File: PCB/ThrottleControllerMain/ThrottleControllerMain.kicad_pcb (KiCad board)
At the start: 2 copper layers, 39 parts, among them J1 Conn_ARM_JTAG_SWD_10, J2 Conn_01x02, J4 Conn_01x04_Pin, J5 Screw_Terminal_01x02, J6 Screw_Terminal_01x02, P1 USB_C_Plug, U1 RP2040, U2 TLV493D, U3 NCP1117-3.3_SOT223, U5 W25Q32JVSS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

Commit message: Updating PCB
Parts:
- C1, C16, C17, C18, C2, C4: footprint Capacitor_SMD:C_0805_2012Metric -> Capacitor_SMD:C_0603_1608Metric
- C11, C12, C13, C14, C15, C5, C6, C7, C8, C9: footprint Capacitor_SMD:C_0805_2012Metric -> Capacitor_SMD:C_0201_0603Metric
- P1: footprint Connector_USB:USB_C_Receptacle_Amphenol_12401548E4-2A -> Connector_USB:USB_C_Receptacle_G-Switch_GT-USB-7010ASV
- R1, R10, R2, R3, R4, R6, R7, R8, R9: footprint Resistor_SMD:R_0805_2012Metric -> Resistor_SMD:R_0603_1608Metric
- moved J4 59.7 mm to (106.2, 84.6), turned to 180 degrees
- moved J1 55.7 mm to (112.3, 76.2), turned to 0 degrees
- moved U2 53.8 mm to (131.1, 80.1)
- moved J2 46.0 mm to (134.6, 109.8), turned to -90 degrees
- moved J6 40.3 mm to (112.5, 69.3)
- moved R7 38.5 mm to (138.4, 103.3), turned to 90 degrees
- moved C3 33.7 mm to (123.3, 82.4), turned to -90 degrees
- moved C10 31.4 mm to (125.9, 82.4), turned to -90 degrees
- moved R5 27.6 mm to (135.9, 72.3)
- moved R2 24.5 mm to (130.8, 75.8), turned to 90 degrees
- moved U3 24.1 mm to (157.5, 99.1)
- moved R9 23.7 mm to (133.3, 75.8), turned to -90 degrees
- moved C17 23.3 mm to (139.1, 89.2), turned to -90 degrees
- moved R8 21.9 mm to (120.4, 82.1), turned to -90 degrees
- moved C14 21.1 mm to (134.6, 80.9)
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
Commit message: PCB footprint layout is mostly complete.
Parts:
- removed J6: Screw_Terminal_01x02, TerminalBlock_Phoenix:TerminalBlock_Phoenix_MPT-0,5-2-2.54_1x02_P2.54mm_Horizontal
- added H1: MountingHole, MountingHole:MountingHole_3.2mm_M3, F.Cu at (159.6, 108.9)
- added H2: MountingHole, MountingHole:MountingHole_3.2mm_M3, F.Cu at (140.2, 69.9)
- added H3: MountingHole, MountingHole:MountingHole_3.2mm_M3, F.Cu at (121.4, 69.9)
- added H4: MountingHole, MountingHole:MountingHole_3.2mm_M3, F.Cu at (140.2, 108.9)
- added J3: Conn_01x02_Socket, Connector_JST:JST_SH_BM02B-SRSS-TB_1x02-1MP_P1.00mm_Vertical, F.Cu at (120.1, 76.6)
- J1: value Conn_ARM_JTAG_SWD_10 -> Conn_01x03_Socket; footprint Connector_PinHeader_2.54mm:PinHeader_2x05_P2.54mm_Vertical -> Connector_JST:JST_SH_BM03B-SRSS-TB_1x03-1MP_P1.00mm_Vertical
- J5: value Screw_Terminal_01x02 -> Conn_01x02_Socket; footprint TerminalBlock_Phoenix:TerminalBlock_Phoenix_MPT-0,5-2-2.54_1x02_P2.54mm_Horizontal -> Connector_JST:JST_SH_BM02B-SRSS-TB_1x02-1MP_P1.00mm_Vertical
- R5: footprint Resistor_SMD:R_0805_2012Metric -> Resistor_SMD:R_0603_1608Metric
- Y1: footprint Crystal:Crystal_SMD_5032-2Pin_5.0x3.2mm -> Crystal:Crystal_SMD_3225-4Pin_3.2x2.5mm
- moved J4 44.0 mm to (148.6, 96.3)
- moved J1 29.9 mm to (142.1, 77.5), turned to -90 degrees
- moved R7 23.7 mm to (126.6, 82.8)
- moved R8 22.5 mm to (142.2, 87.8), turned to 180 degrees
- moved C5 22.4 mm to (136.7, 80.9), turned to 90 degrees
- moved C1 20.0 mm to (157.6, 104.3), turned to 0 degrees
- moved C16 19.8 mm to (142.2, 86.0), turned to 0 degrees
- moved R4 19.3 mm to (138.6, 94.5)
- moved R3 19.1 mm to (136.7, 94.5)
- moved R1 17.3 mm to (125.9, 74.8), turned to 0 degrees
- moved Y1 14.4 mm to (134.3, 72.8)
- moved R10 14.3 mm to (125.9, 76.7), turned to 180 degrees
- moved C15 11.5 mm to (135.7, 76.4), turned to 90 degrees
- moved J5 10.2 mm to (120.1, 83.2), turned to 90 degrees
- moved C7 9.52 mm to (140.3, 101.3), turned to 180 degrees
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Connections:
- J1 pad 1: +3.3V -> GND
- J1 pad 3: GND -> Net-(J1-Pin_3)
- R10 pad 2: Net-(J6-Pin_1) -> Net-(J5-Pin_1)
- R5 pad 2: Net-(J1-~{RESET}) -> Net-(U1-RUN)
- R9 pad 2: Net-(J5-Pin_1) -> Net-(J3-Pin_1)
- U1 pad 24: Net-(J1-SWDCLK/TCK) -> Net-(J1-Pin_3)
- U1 pad 26: Net-(J1-~{RESET}) -> Net-(U1-RUN)
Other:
- board outline added: 45.3 x 46 mm

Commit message: PCB positioning improvements
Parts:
- C13, C5, C6, C7, C8, C9: footprint Capacitor_SMD:C_0201_0603Metric -> Capacitor_SMD:C_0805_2012Metric
- C4: footprint Capacitor_SMD:C_0603_1608Metric -> Capacitor_SMD:C_0805_2012Metric
- moved C13 4.68 mm to (143.9, 101.3)
- moved C17 3.30 mm to (141.9, 91.2)
- moved C2 3.20 mm to (141.9, 93.2)
- moved C4 2.90 mm to (141.8, 95.4)
- moved C7 2.80 mm to (139.6, 98.6)
- moved C9 2.42 mm to (139.6, 101.0)
- moved C8 1.31 mm to (139.7, 103.4)
- moved C15 1.02 mm to (136.4, 77.1)
- moved C6 0.94 mm to (134.3, 77.3)

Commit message: Added serial-port debug header.
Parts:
- added J6: Conn_01x03, Connector_PinHeader_2.54mm:PinHeader_1x03_P2.54mm_Vertical, F.Cu at (145.8, 100.5)
- J4: footprint Connector_JST:JST_SH_SM04B-SRSS-TB_1x04-1MP_P1.00mm_Horizontal -> Connector_JST:JST_SH_BM04B-SRSS-TB_1x04-1MP_P1.00mm_Vertical
- moved C13 4.56 mm to (139.8, 103.3)
- moved C7 4.29 mm to (141.6, 94.8)
- moved C17 3.11 mm to (141.7, 88.1)
- moved C2 3.11 mm to (141.7, 90.1)
- moved C4 3.11 mm to (141.7, 92.3)
- moved C8 2.50 mm to (139.8, 100.9)
- moved C9 2.50 mm to (139.8, 98.5)
- moved C16 1.65 mm to (141.8, 84.4)
- moved C18 1.65 mm to (141.8, 82.5)
- moved R8 1.65 mm to (141.8, 86.2)
- moved J4 0.68 mm to (148.7, 95.6), turned to 0 degrees
- moved U3 0.57 mm to (157.6, 98.8)
- moved P1 0.25 mm to (149.9, 107.8)
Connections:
- U1 pad 6: unconnected-(U1-GPIO4-Pad6) -> Net-(J6-Pin_1)
- U1 pad 7: unconnected-(U1-GPIO5-Pad7) -> Net-(J6-Pin_2)

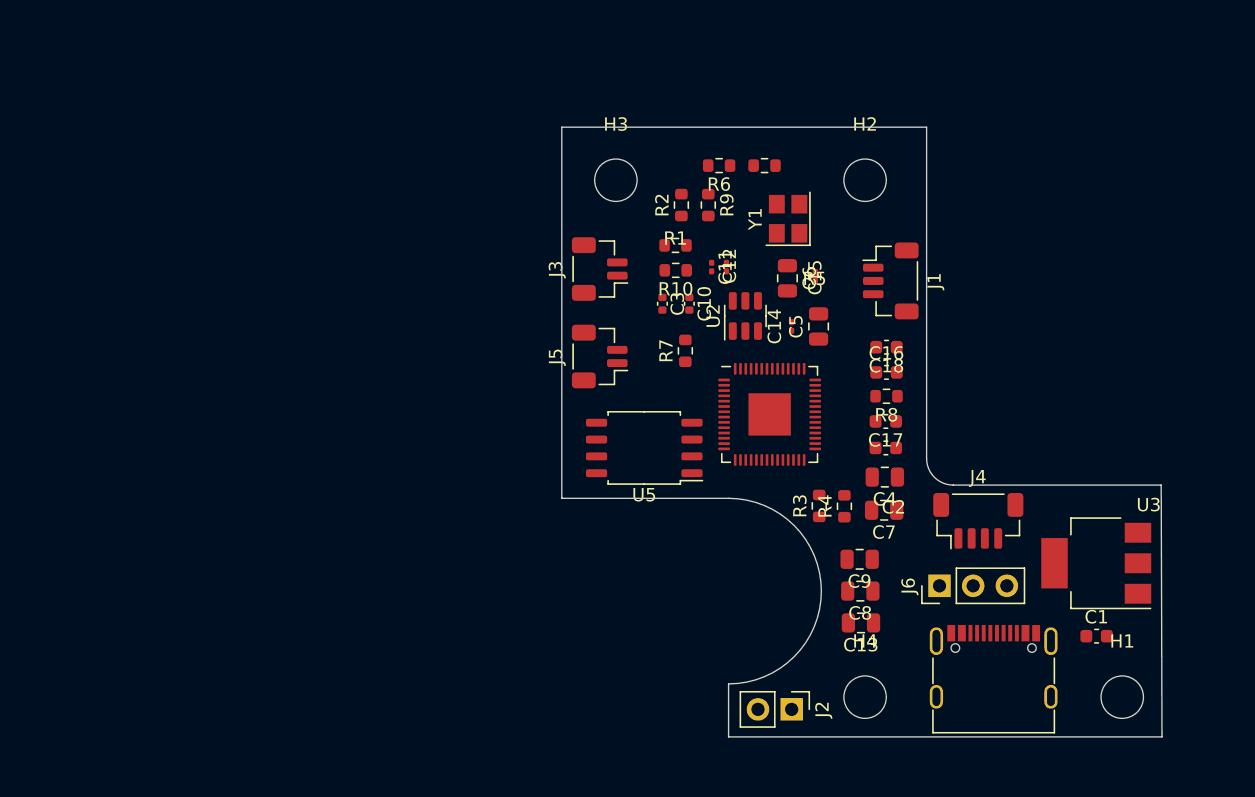
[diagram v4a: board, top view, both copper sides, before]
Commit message: Finished first draft of routing.
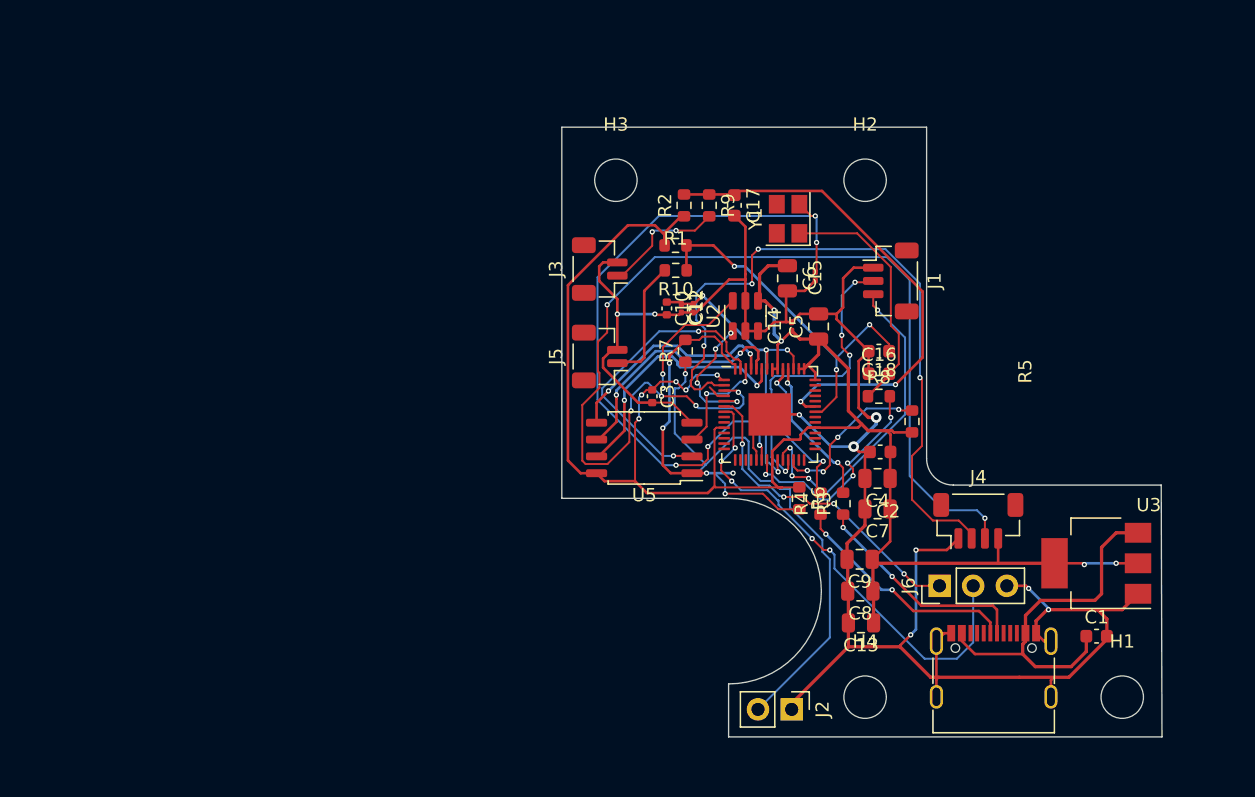
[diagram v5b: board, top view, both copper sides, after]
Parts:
- moved R6 25.8 mm to (135.2, 93.9), turned to -90 degrees
- moved R5 22.3 mm to (143.7, 88.1), turned to 90 degrees
- moved C17 19.9 mm to (130.3, 71.8), turned to -90 degrees
- moved C3 7.02 mm to (124.1, 86.2)
- moved C12 3.98 mm to (127.2, 79.6)
- moved C11 3.85 mm to (126.3, 79.6)
- moved R4 1.81 mm to (136.8, 94.3)
- moved R3 1.81 mm to (138.5, 94.3)
- moved C10 1.74 mm to (125.2, 79.6)
- moved C18 0.65 mm to (141.2, 82.8)
- moved C16 0.58 mm to (141.2, 84.5)
- moved R8 0.58 mm to (141.2, 86.2), turned to 0 degrees
- moved C4 0.56 mm to (141.1, 92.4)
- moved C2 0.52 mm to (141.3, 90.4)
- moved C7 0.51 mm to (141.1, 94.7)
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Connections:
- U5 pad 2: unconnected-(U5-DO(IO1)-Pad2) -> /QSPI_SD1
- U5 pad 3: unconnected-(U5-IO2-Pad3) -> /QSPI_SD2
- U5 pad 5: unconnected-(U5-DI(IO0)-Pad5) -> /QSPI_SDO
- U5 pad 6: unconnected-(U5-CLK-Pad6) -> /QSPI_SCLK
- U5 pad 7: unconnected-(U5-IO3-Pad7) -> /QSPI_SD3
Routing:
- net GND: track 0.00 -> 164.7 mm, vias 0 -> 9
- net +3.3V: track 0.00 -> 144.4 mm, vias 0 -> 9
- net Net-(J4-Pin_3): track 0.00 -> 80.8 mm, vias 0 -> 6
- net Net-(J4-Pin_2): track 0.00 -> 53.8 mm, vias 0 -> 4
- net Net-(U1-XIN): track 0.00 -> 52.3 mm, vias 0 -> 5
- net Net-(J2-Pin_2): track 0.00 -> 40.4 mm, vias 0 -> 1
- net Net-(U1-GPIO25): track 0.00 -> 38.1 mm, vias 0 -> 2
- net Net-(J6-Pin_2): track 0.00 -> 36.1 mm, vias 0 -> 5
- net /QSPI_SS: track 0.00 -> 29.7 mm, vias 0 -> 5
- net +5V: track 0.00 -> 28.5 mm
- net Net-(U1-GPIO24): track 0.00 -> 27.9 mm, vias 0 -> 3
- net +1V1: track 0.00 -> 25.2 mm, vias 0 -> 4
- net Net-(J1-Pin_3): track 0.00 -> 25.0 mm, vias 0 -> 4
- net Net-(J6-Pin_1): track 0.00 -> 24.2 mm, vias 0 -> 4
- net /QSPI_SD1: track 0.00 -> 23.3 mm, vias 0 -> 2
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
